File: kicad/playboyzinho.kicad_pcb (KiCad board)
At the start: 2 copper layers, 143.2 x 213 mm, 16 parts, among them SW1 SW_Push, SW2 SW_Push, SW3 SW_Push, SW4 SW_Push, SW5 SW_Push, SW6 SW_Push, SW7 SW_Push, SW8 SW_Push, SW9 SW_SPDT, U1 esp32-s3-pl, U7 (amplificador)_MAX98357_Module

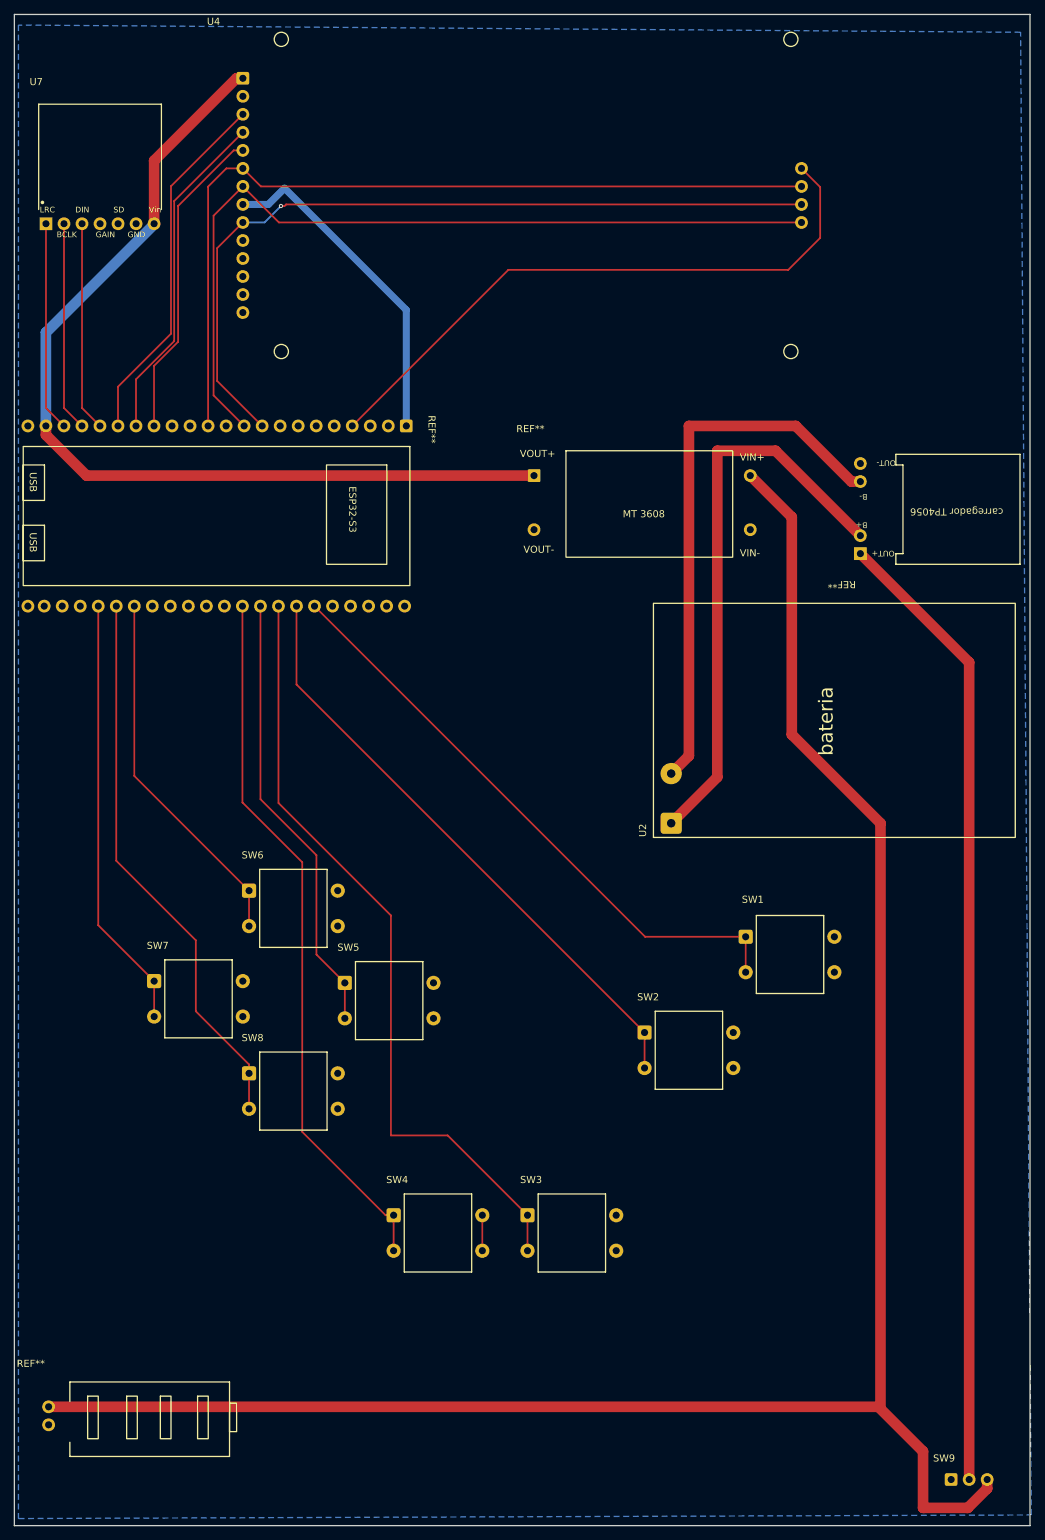
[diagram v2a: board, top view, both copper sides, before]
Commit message: fix: corrige indicador de bateria errado e faz pequenos ajustes
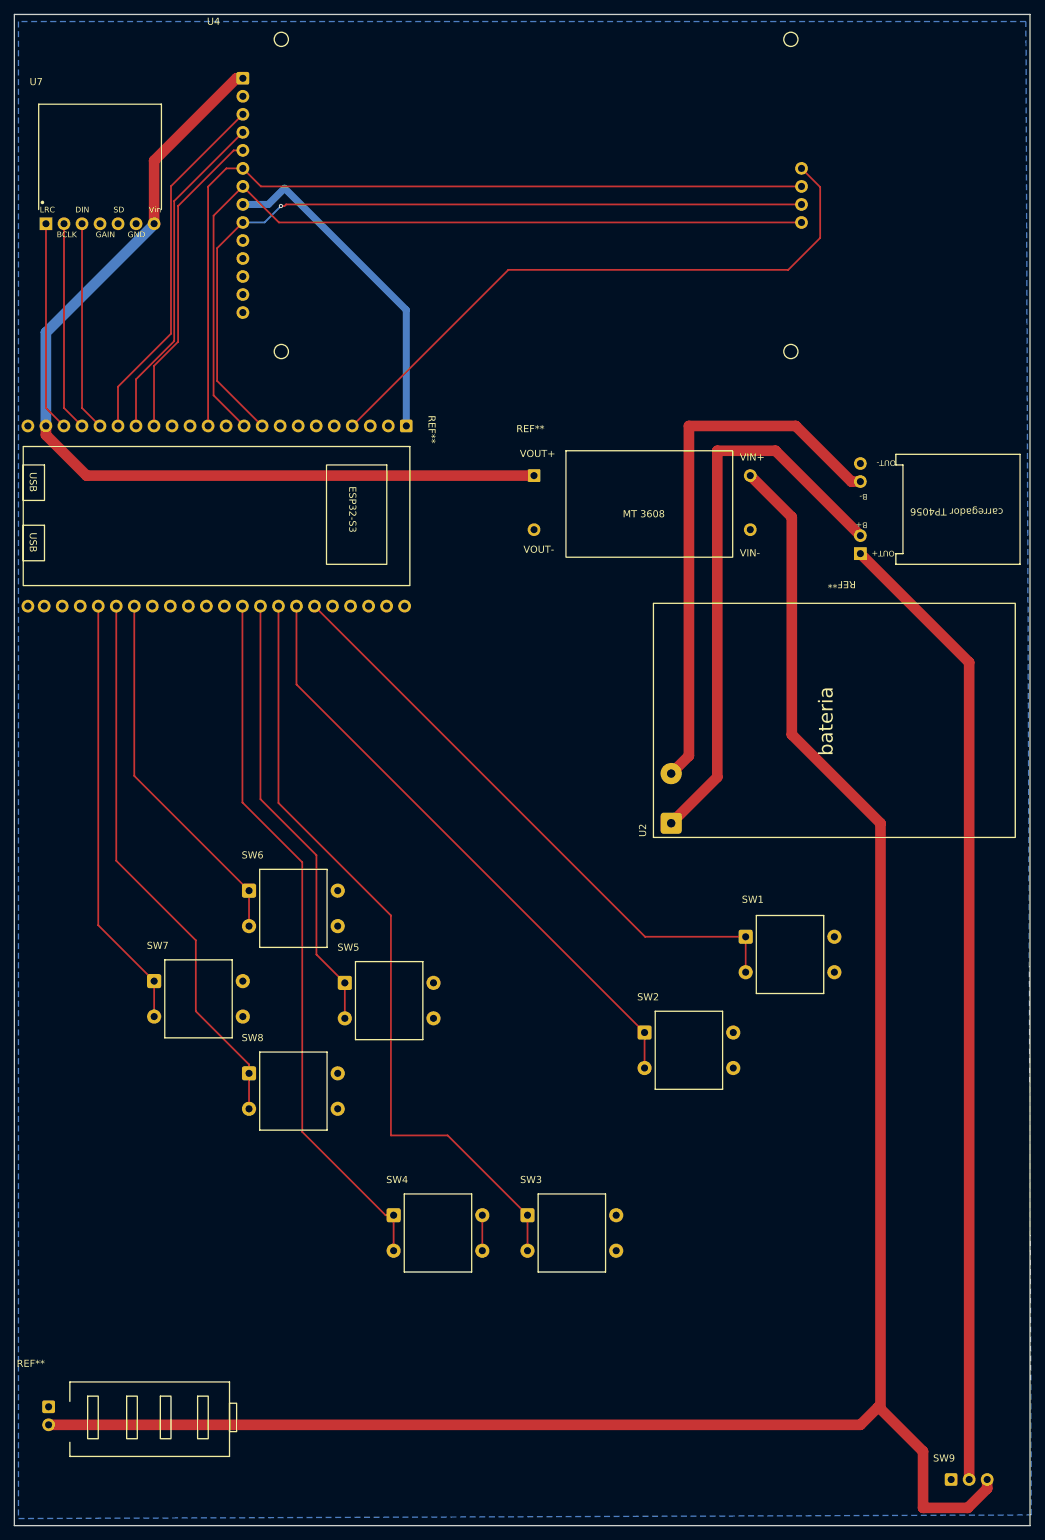
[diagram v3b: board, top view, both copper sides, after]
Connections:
- U6 pad 1: Net-(SW9-C) -> GND
- U6 pad 2: GND -> Net-(SW9-C)
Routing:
- net Net-(SW9-C): track 284.2 -> 285.4 mm
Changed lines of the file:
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@@
 		(sheetname "/")
 		(sheetfile "playboyzinho.kicad_sch")
-		(units
-			(unit
-				(name "A")
-				(pins "1" "2" "3" "4" "5" "6" "7")
-			)
-		)
 		(attr smd)
 		(duplicate_pad_numbers_are_jumpers no)
@@
 			)
 		)
+		(fp_text user ""
+			(at -11 -8 0)
+			(unlocked yes)
+			(layer "F.Fab")
+			(effects
+				(font
+					(size 1 1)
+					(thickness 0.15)
+				)
+			)
+		)
 		(fp_text user "${REFERENCE}"
 			(at 2.5 -7.5 0)
@@
 		(sheetname "/")
 		(sheetfile "playboyzinho.kicad_sch")
-		(units
-			(unit
-				(name "A")
-				(pins "1" "2")
-			)
-		)
 		(attr smd)
 		(duplicate_pad_numbers_are_jumpers no)
@@
 		(sheetname "/")
 		(sheetfile "playboyzinho.kicad_sch")
-		(units
-			(unit
-				(name "A")
-				(pins "1" "2" "3" "4" "5" "6" "7" "8" "9" "10" "11" "12" "13" "14" "15"
-					"16" "17" "18" "19" "20" "21" "22" "23" "24" "25" "26" "27" "28" "29"
-					"30" "31" "32" "33" "34" "35" "36" "37" "38" "39" "40" "41" "42" "43"
-					"44"
-				)
-			)
-		)
 		(attr smd)
 		(duplicate_pad_numbers_are_jumpers no)
@@
 		(sheetname "/")
 		(sheetfile "playboyzinho.kicad_sch")
-		(units
-			(unit
-				(name "A")
-				(pins "1" "2")
-			)
-		)
 		(attr smd)
 		(duplicate_pad_numbers_are_jumpers no)
@@
 		(sheetname "/")
 		(sheetfile "playboyzinho.kicad_sch")
-		(units
-			(unit
-				(name "A")
-				(pins "5" "6" "1" "2" "3" "4")
-			)
-		)
 		(attr smd)
 		(duplicate_pad_numbers_are_jumpers no)
@@
 		(sheetname "/")
 		(sheetfile "playboyzinho.kicad_sch")
-		(units
-			(unit
-				(name "A")
-				(pins "1" "2")
-			)
-		)
 		(attr smd)
 		(duplicate_pad_numbers_are_jumpers no)
@@
 		(sheetname "/")
 		(sheetfile "playboyzinho.kicad_sch")
-		(units
-			(unit
-				(name "A")
-				(pins "1" "2")
-			)
-		)
 		(attr smd)
 		(duplicate_pad_numbers_are_jumpers no)
@@
 		(sheetname "/")
 		(sheetfile "playboyzinho.kicad_sch")
-		(units
-			(unit
-				(name "A")
-				(pins "1" "2")
-			)
-		)
 		(attr smd)
 		(duplicate_pad_numbers_are_jumpers no)
@@
 		(sheetname "/")
 		(sheetfile "playboyzinho.kicad_sch")
-		(units
-			(unit
-				(name "A")
-				(pins "1" "2" "3" "4")
-			)
-		)
 		(attr smd)
 		(duplicate_pad_numbers_are_jumpers no)
@@
 		(sheetname "/")
 		(sheetfile "playboyzinho.kicad_sch")
-		(units
-			(unit
-				(name "A")
-				(pins "1" "2")
-			)
-		)
 		(attr smd)
 		(duplicate_pad_numbers_are_jumpers no)
@@
 			)
 		)
-		(pad "1" thru_hole circle
+		(pad "1" thru_hole roundrect
 			(at 0 0)
 			(size 1.8 1.8)
@@
 			(layers "*.Cu" "*.Mask")
 			(remove_unused_layers no)
-			(net "Net-(SW9-C)")
-			(pinfunction "BAT+_1")
-			(pintype "power_in")
+			(roundrect_rratio 0.1388888889)
+			(net "GND")
+			(pinfunction "BAT-_1")
+			(pintype "passive")
+			(thermal_bridge_angle 45)
 		)
 		(pad "2" thru_hole circle
@@
 			(layers "*.Cu" "*.Mask")
 			(remove_unused_layers no)
-			(net "GND")
-			(pinfunction "BAT-_2")
-			(pintype "passive")
+			(net "Net-(SW9-C)")
+			(pinfunction "BAT+_2")
+			(pintype "power_in")
 		)
 		(embedded_fonts no)
@@
 		(sheetname "/")
 		(sheetfile "playboyzinho.kicad_sch")
-		(units
-			(unit
-				(name "A")
-				(pins "1" "2")
-			)
-		)
 		(attr smd)
 		(duplicate_pad_numbers_are_jumpers no)
@@
 		(sheetname "/")
 		(sheetfile "playboyzinho.kicad_sch")
-		(units
-			(unit
-				(name "A")
-				(pins "1" "2")
-			)
-		)
 		(attr smd)
 		(duplicate_pad_numbers_are_jumpers no)
@@
 		(sheetname "/")
 		(sheetfile "playboyzinho.kicad_sch")
-		(units
-			(unit
-				(name "A")
-				(pins "2" "1" "3")
-			)
-		)
 		(attr smd)
 		(duplicate_pad_numbers_are_jumpers no)
@@
 		(sheetname "/")
 		(sheetfile "playboyzinho.kicad_sch")
-		(units
-			(unit
-				(name "A")
-				(pins "1" "2" "3" "4" "5" "6" "7" "8" "9" "10" "11" "12" "13" "14" "15"
-					"16" "17" "18"
-				)
-			)
-		)
 		(attr smd)
 		(duplicate_pad_numbers_are_jumpers no)
@@
 		(sheetname "/")
 		(sheetfile "playboyzinho.kicad_sch")
-		(units
-			(unit
-				(name "A")
-				(pins "1" "2")
-			)
-		)
 		(attr smd)
 		(duplicate_pad_numbers_are_jumpers no)
@@
 		(sheetname "/")
 		(sheetfile "playboyzinho.kicad_sch")
-		(units
-			(unit
-				(name "A")
-				(pins "1" "2")
-			)
-		)
 		(attr smd)
 		(duplicate_pad_numbers_are_jumpers no)
@@
 	)
 	(segment
-		(start -17.303704 199.79)
-		(end -17.38 199.79)
-		(width 1.5)
-		(layer "B.Cu")
-		(net "GND")
-	)
-	(segment
 		(start -17.7615 59)
 		(end -17.7615 60.272792)
@@
 	)
 	(segment
-		(start -17.38 197.25)
-		(end 99.58 197.25)
-		(width 1.5)
-		(layer "F.Cu")
-		(net "Net-(SW9-C)")
-	)
-	(segment
 		(start 105.87 203.54)
 		(end 105.87 211.5)
@@
 	)
 	(segment
+		(start 97.04 199.79)
+		(end 99.58 197.25)
+		(width 1.5)
+		(layer "F.Cu")
+		(net "Net-(SW9-C)")
+	)
+	(segment
 		(start 112.182792 211.5)
 		(end 114.91 208.772792)
@@
 	)
 	(segment
+		(start -17.38 199.79)
+		(end 97.04 199.79)
+		(width 1.5)
+		(layer "F.Cu")
+		(net "Net-(SW9-C)")
+	)
+	(segment
 		(start 99.58 197.25)
 		(end 105.87 203.54)
@@
 		(net "Net-(SW9-C)")
 	)
+	(segment
+		(start -17.303704 199.79)
+		(end -17.38 199.79)
+		(width 1.5)
+		(layer "B.Cu")
+		(net "Net-(SW9-C)")
+	)
 	(zone
 		(net "GND")
@@
 		(polygon
 			(pts
-				(xy -21.63 2.496403) (xy -21.63 213.001779) (xy 121.119955 212.493772) (xy 119.62009 3.512591)
+				(xy -21.63 2) (xy -21.63 213.001779) (xy 121.119955 212.493772) (xy 120.37 2)
 			)
 		)

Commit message: refact: ajustes de tamanho do pcb e posicionamento dos botões
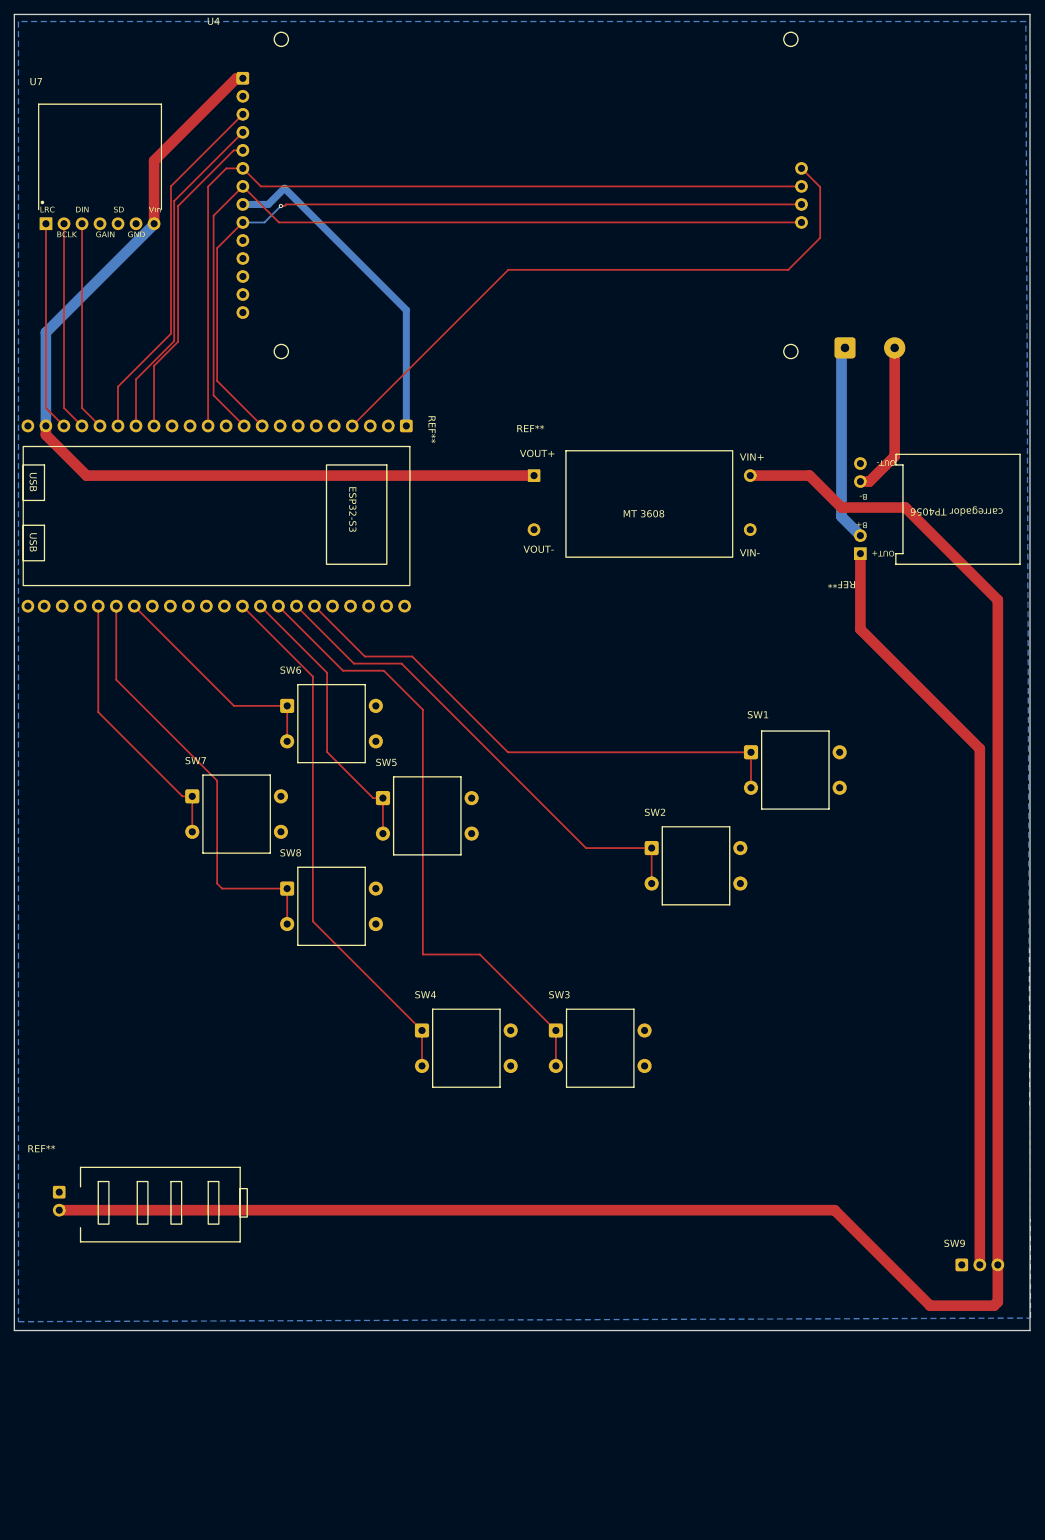
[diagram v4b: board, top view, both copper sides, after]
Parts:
- U2: moved to B.Cu
- moved U2 71.3 mm to (94.9, 48.0), turned to 0 degrees
- moved SW9 30.3 mm to (111.3, 177.2)
- moved U6 30.3 mm to (-15.9, 167.0)
- moved SW5 26.6 mm to (29.7, 111.5)
- moved SW6 26.6 mm to (16.2, 98.5)
- moved SW7 26.6 mm to (2.87, 111.2)
- moved SW8 26.6 mm to (16.2, 124.2)
- moved SW3 26.3 mm to (54.1, 144.2)
- moved SW4 26.3 mm to (35.2, 144.2)
- moved SW2 26.0 mm to (67.6, 118.5)
- moved SW1 26.0 mm to (81.6, 105.0)
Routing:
- net -BATT: track 77.5 -> 21.6 mm
- net +BATT: track 80.3 -> 27.8 mm
- net Net-(SW9-B): track 136.9 -> 107.2 mm
- net /Button-4: track 100.3 -> 75.3 mm
- net /Button-5: track 63.0 -> 40.0 mm
- net /Button-7: track 61.1 -> 38.1 mm
- net /Button-3: track 110.1 -> 89.1 mm
- net /Button-6: track 51.8 -> 32.4 mm
- net /Button-8: track 78.6 -> 60.2 mm
- net /Button-2: track 85.4 -> 69.2 mm
- net /Button-1: track 85.1 -> 75.1 mm
- net Net-(SW9-C): track 285.4 -> 279.2 mm
- net GND: track 5.00 -> 0.00 mm
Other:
- board size 143.2 x 213 mm -> 143.2 x 185.5 mm

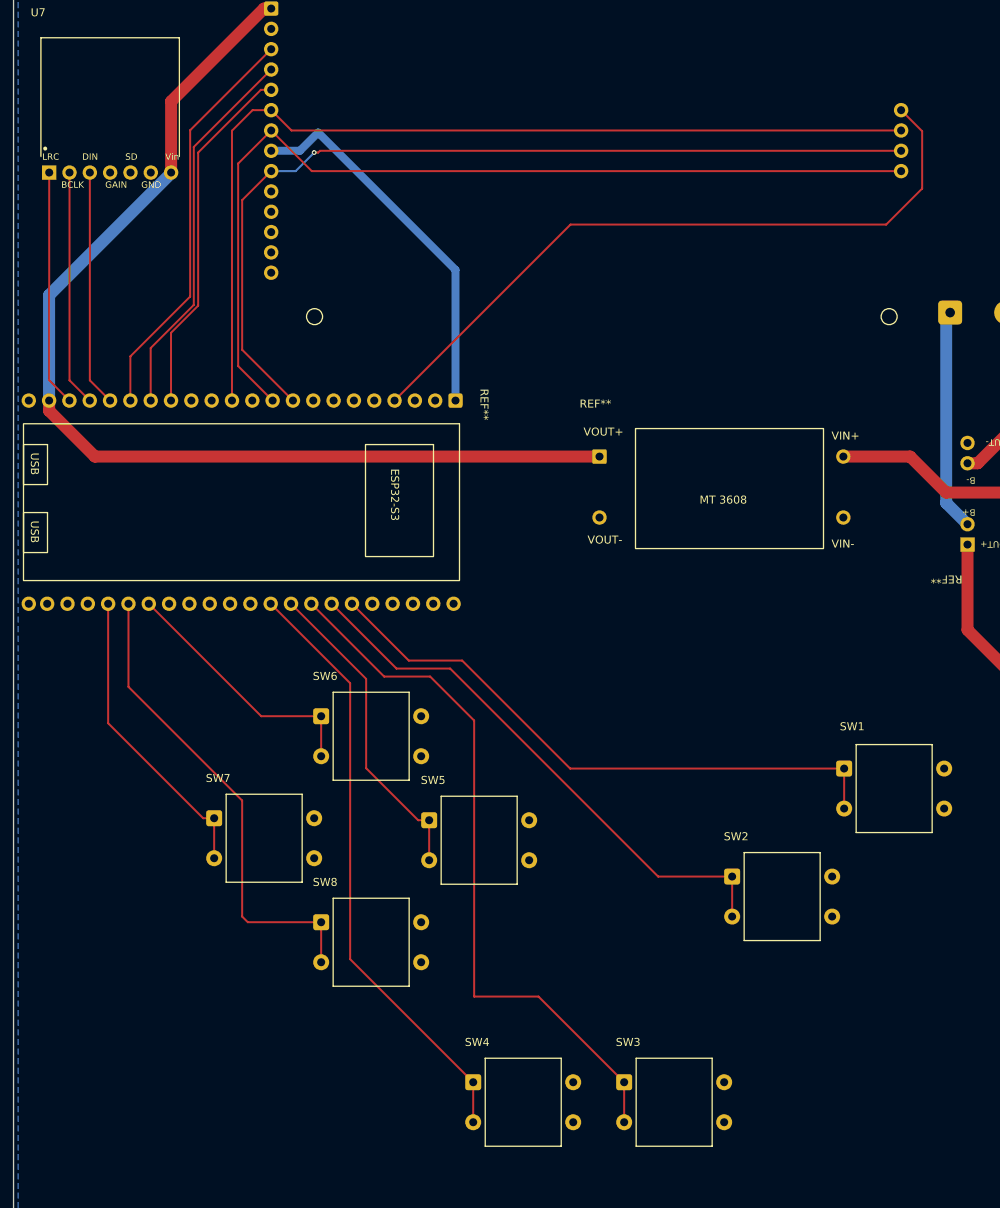
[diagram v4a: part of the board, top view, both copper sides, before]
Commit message: refact: altera par de botões conectados e muda gpios para 0,3mm
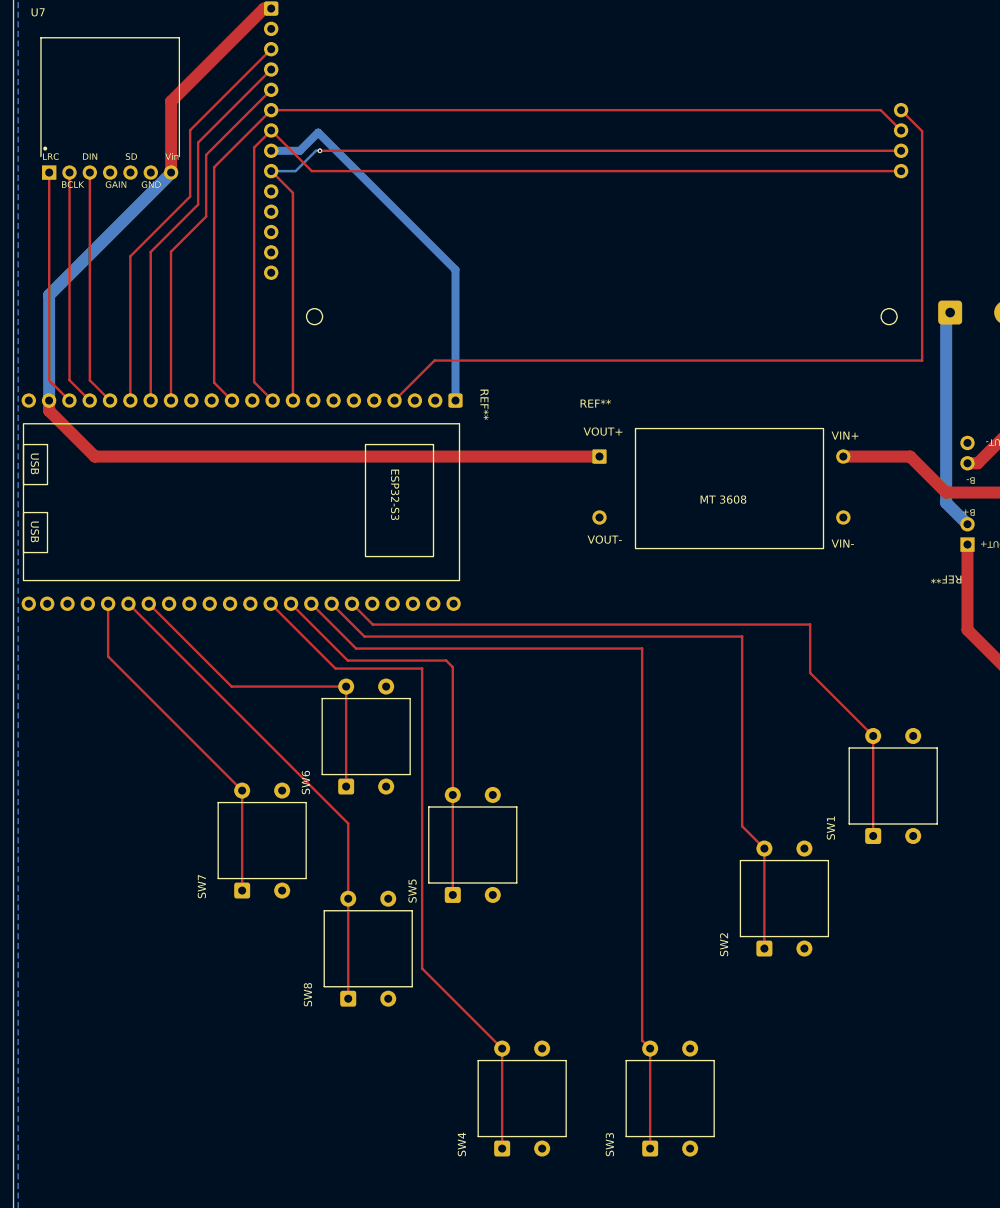
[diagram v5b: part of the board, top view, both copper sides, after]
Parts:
- moved SW8 10.1 mm to (19.6, 133.8), turned to 90 degrees
- moved SW2 9.86 mm to (71.7, 127.5), turned to 90 degrees
- moved SW5 9.80 mm to (32.7, 120.8), turned to 90 degrees
- moved SW7 9.69 mm to (6.37, 120.2), turned to 90 degrees
- moved SW6 9.33 mm to (19.4, 107.2), turned to 90 degrees
- moved SW1 9.18 mm to (85.2, 113.4), turned to 90 degrees
- moved SW4 9.05 mm to (38.9, 152.5), turned to 90 degrees
- moved SW3 8.90 mm to (57.4, 152.5), turned to 90 degrees
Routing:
- net /Button-2: track 69.2 -> 93.2 mm
- net /Button-3: track 89.1 -> 106.6 mm
- net /Button-1: track 75.1 -> 88.0 mm
- net /SD_CS: track 87.8 -> 100.4 mm
- net /Button-5: track 40.0 -> 52.0 mm
- net /Button-4: track 75.3 -> 86.4 mm
- net /Button-6: track 32.4 -> 41.5 mm
- net /Button-7: track 38.1 -> 42.8 mm
- net /MISO: track 112.6 -> 109.6 mm
- net /SCK: track 118.1 -> 116.4 mm
- net /DC: track 44.8 -> 44.0 mm
- net /Button-8: track 60.2 -> 60.7 mm
